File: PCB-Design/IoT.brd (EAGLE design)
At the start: 59.7 x 51.7 mm, 11 parts, among them M2 ARDUINO-NANO-3.0, M3 WIRELESS-NRF24L01

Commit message: PCB edit
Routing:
- net N$15: track 41.6 -> 39.6 mm
- net VCC: track 78.5 -> 76.5 mm
- net GND: track 105.4 -> 104.3 mm
- net N$9: track 50.2 -> 49.4 mm
- net N$13: track 17.7 -> 16.9 mm
- net N$12: track 17.7 -> 16.9 mm
- added copper zone on layer 1, net GND
- added copper zone on layer 16, net GND

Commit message: Redone PCB on bottom only
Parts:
- C1, C2: value (none) -> 10U/35V; device resistor:C025-040X050 -> capacitors-electrolytic:E2-5
- moved U$6 51.4 mm to (5.08, 78.7), turned to 0 degrees
- moved C1 14.0 mm to (24.1, 83.8), turned to 0 degrees
- moved HC-SR04-1 10.5 mm to (16.5, 55.9)
- moved M2 10.2 mm to (33.0, 69.8)
- moved HC-SR04-2 9.25 mm to (27.9, 55.9)
- moved HC-SR04-3 8.03 mm to (39.4, 55.9)
- moved C2 7.62 mm to (24.1, 94.0), turned to 0 degrees
- moved HC-SR04-4 6.84 mm to (50.8, 55.9)
- moved R1 3.81 mm to (19.1, 88.9)
- moved M3 2.84 mm to (43.2, 88.9)
- moved U$5 2.54 mm to (7.62, 92.7)
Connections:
- removed net N$4: C1.1, C2.1, M2.J2.14, M3.2
- new net N$2: C1.+, C2.+, M2.J2.14, M3.2
- net GND: now also C1.-, C2.-; no longer C1.2, C2.2
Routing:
- net GND: track 104.3 -> 0.00 mm, vias 1 -> 0
- net N$9: track 49.4 -> 147.9 mm
- net N$2: track 0.00 -> 47.6 mm
- net N$4: track 34.7 -> 0.00 mm
- net VCC: track 76.5 -> 104.5 mm
- net N$16: track 18.7 -> 30.2 mm
- net N$17: track 31.9 -> 43.2 mm
- net N$15: track 39.6 -> 46.7 mm
- net N$11: track 12.3 -> 7.40 mm
- net N$10: track 12.3 -> 7.40 mm
- net N$1: track 51.1 -> 46.2 mm
- net N$12: track 16.9 -> 12.3 mm
- net N$14: track 18.1 -> 22.5 mm
- net N$8: track 11.2 -> 7.93 mm
- net N$7: track 11.2 -> 7.93 mm
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- removed copper zone on layer 1, net GND
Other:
- board size 59.7 x 51.7 mm -> 60.9 x 49.2 mm

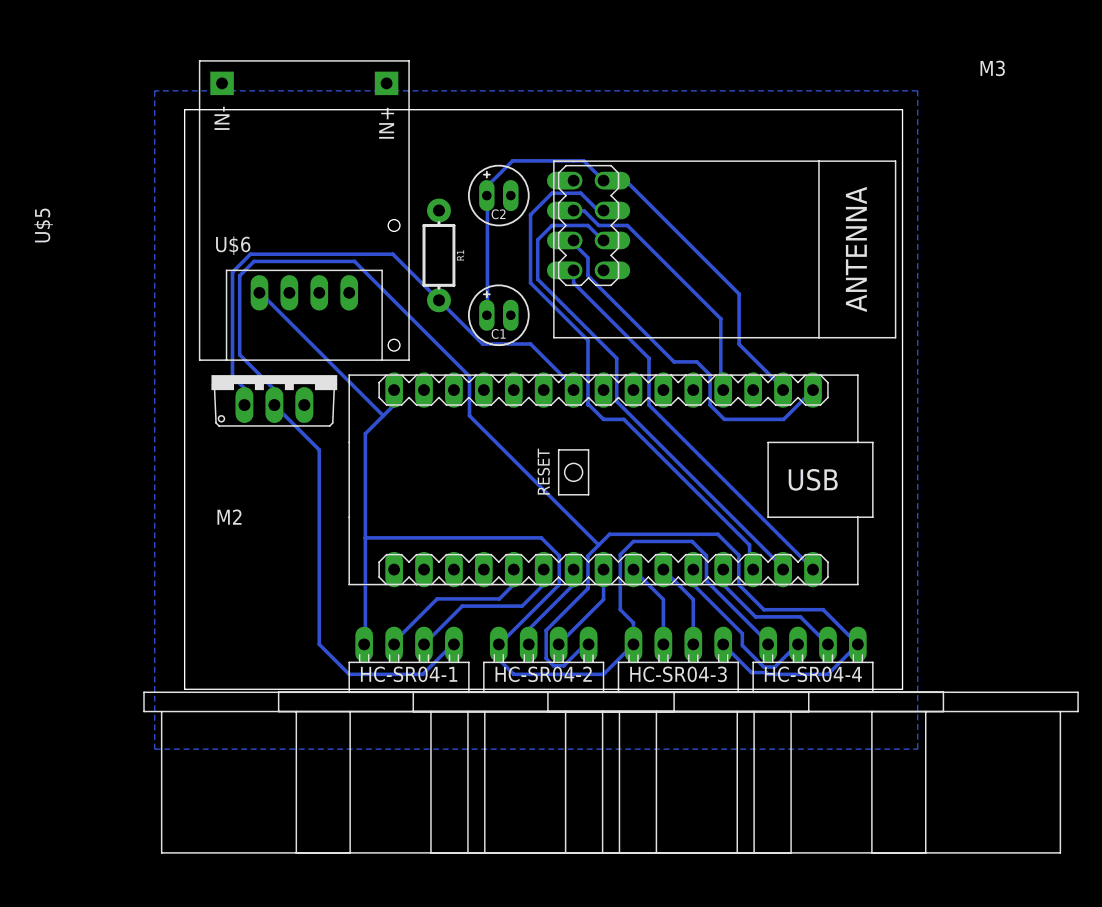
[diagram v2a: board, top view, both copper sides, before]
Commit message: New PCB no wires necessary
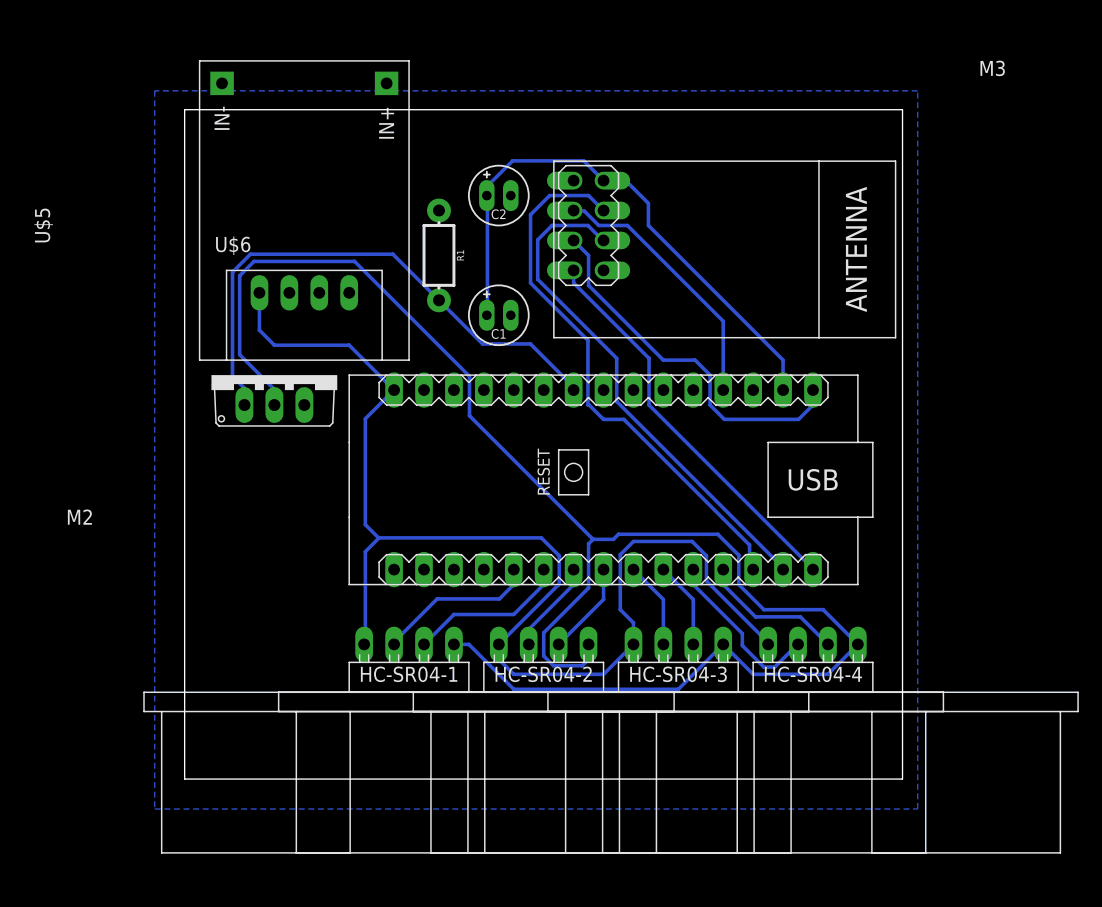
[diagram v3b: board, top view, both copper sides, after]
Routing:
- net N$9: track 147.9 -> 139.3 mm
- net VCC: track 104.5 -> 106.4 mm
- net N$16: track 30.2 -> 31.4 mm
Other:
- board size 60.9 x 49.2 mm -> 60.9 x 56.8 mm
- board text added: "Wits ParkSmart IoT"

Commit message: PCB edit
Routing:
- net N$9: track 139.3 -> 140.4 mm
- net VCC: track 106.4 -> 107.2 mm
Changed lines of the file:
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@@
 <layer number="19" name="Unrouted" color="6" fill="1" visible="yes" active="yes"/>
 <layer number="20" name="Dimension" color="24" fill="1" visible="yes" active="yes"/>
-<layer number="21" name="tPlace" color="7" fill="1" visible="yes" active="yes"/>
-<layer number="22" name="bPlace" color="7" fill="1" visible="yes" active="yes"/>
+<layer number="21" name="tPlace" color="7" fill="1" visible="no" active="yes"/>
+<layer number="22" name="bPlace" color="7" fill="1" visible="no" active="yes"/>
 <layer number="23" name="tOrigins" color="15" fill="1" visible="yes" active="yes"/>
 <layer number="24" name="bOrigins" color="15" fill="1" visible="yes" active="yes"/>
-<layer number="25" name="tNames" color="7" fill="1" visible="yes" active="yes"/>
+<layer number="25" name="tNames" color="7" fill="1" visible="no" active="yes"/>
 <layer number="26" name="bNames" color="7" fill="1" visible="yes" active="yes"/>
-<layer number="27" name="tValues" color="7" fill="1" visible="yes" active="yes"/>
-<layer number="28" name="bValues" color="7" fill="1" visible="yes" active="yes"/>
+<layer number="27" name="tValues" color="7" fill="1" visible="no" active="yes"/>
+<layer number="28" name="bValues" color="7" fill="1" visible="no" active="yes"/>
 <layer number="29" name="tStop" color="7" fill="3" visible="no" active="yes"/>
 <layer number="30" name="bStop" color="7" fill="6" visible="no" active="yes"/>
@@
 <contactref element="HC-SR04-1" pad="4"/>
 <contactref element="U$6" pad="2"/>
-<wire x1="46.6344" y1="58.8264" x2="44.5008" y2="60.96" width="0.3048" layer="16"/>
-<wire x1="54.5592" y1="55.7784" x2="54.61" y2="55.88" width="0.3048" layer="16"/>
-<wire x1="21.6408" y1="78.6384" x2="21.6408" y2="75.2856" width="0.3048" layer="16"/>
-<wire x1="11.8872" y1="88.392" x2="21.6408" y2="78.6384" width="0.3048" layer="16"/>
+<wire x1="21.6408" y1="78.6384" x2="11.8872" y2="88.392" width="0.3048" layer="16"/>
 <wire x1="3.3528" y1="88.392" x2="11.8872" y2="88.392" width="0.3048" layer="16"/>
 <wire x1="2.1336" y1="87.1728" x2="3.3528" y2="88.392" width="0.3048" layer="16"/>
@@
 <wire x1="2.1336" y1="80.4672" x2="5.08" y2="77.5208" width="0.3048" layer="16"/>
 <wire x1="5.08" y1="77.5208" x2="5.08" y2="76.2" width="0.3048" layer="16"/>
-<wire x1="44.5008" y1="63.4492" x2="44.5008" y2="60.96" width="0.3048" layer="16"/>
+<wire x1="44.5008" y1="60.96" x2="44.5008" y2="63.4492" width="0.3048" layer="16"/>
 <wire x1="42.7228" y1="65.2272" x2="44.5008" y2="63.4492" width="0.3048" layer="16"/>
-<wire x1="52.07" y1="53.34" x2="54.5084" y2="55.7784" width="0.3048" layer="16"/>
-<wire x1="54.5084" y1="55.7784" x2="54.5592" y2="55.7784" width="0.3048" layer="16"/>
-<wire x1="54.61" y1="55.88" x2="51.6636" y2="58.8264" width="0.3048" layer="16"/>
-<wire x1="51.6636" y1="58.8264" x2="46.6344" y2="58.8264" width="0.3048" layer="16"/>
 <wire x1="31.75" y1="55.88" x2="31.75" y2="54.61" width="0.3048" layer="16"/>
 <wire x1="28.771425" y1="54.0672" x2="27.94" y2="54.898625" width="0.3048" layer="16"/>
@@
 <wire x1="31.2072" y1="54.0672" x2="31.75" y2="54.61" width="0.3048" layer="16"/>
 <wire x1="43.18" y1="55.88" x2="45.72" y2="53.34" width="0.3048" layer="16"/>
-<wire x1="45.72" y1="53.34" x2="52.07" y2="53.34" width="0.3048" layer="16"/>
-<wire x1="39.37" y1="52.07" x2="43.18" y2="55.88" width="0.3048" layer="16"/>
-<wire x1="25.4" y1="52.07" x2="39.37" y2="52.07" width="0.3048" layer="16"/>
+<wire x1="43.18" y1="55.88" x2="40.005" y2="52.705" width="0.3048" layer="16"/>
 <wire x1="20.32" y1="55.88" x2="21.59" y2="55.88" width="0.3048" layer="16"/>
-<wire x1="21.59" y1="55.88" x2="25.4" y2="52.07" width="0.3048" layer="16"/>
-<wire x1="21.6408" y1="75.2856" x2="32.131" y2="64.7954" width="0.3048" layer="16"/>
+<wire x1="24.765" y1="52.705" x2="21.59" y2="55.88" width="0.3048" layer="16"/>
 <wire x1="34.29" y1="65.2272" x2="42.7228" y2="65.2272" width="0.3048" layer="16"/>
-<wire x1="31.75" y1="64.4144" x2="32.131" y2="64.7954" width="0.3048" layer="16"/>
 <wire x1="27.94" y1="56.861375" x2="31.75" y2="60.671375" width="0.3048" layer="16"/>
-<wire x1="31.75" y1="60.671375" x2="31.75" y2="64.4144" width="0.3048" layer="16"/>
-<wire x1="33.8582" y1="64.7954" x2="34.29" y2="65.2272" width="0.3048" layer="16"/>
-<wire x1="32.131" y1="64.7954" x2="33.8582" y2="64.7954" width="0.3048" layer="16"/>
+<wire x1="31.75" y1="60.671375" x2="31.75" y2="63.5" width="0.3048" layer="16"/>
+<wire x1="31.75" y1="63.5" x2="32.385" y2="64.135" width="0.3048" layer="16"/>
+<wire x1="32.385" y1="64.135" x2="33.02" y2="64.77" width="0.3048" layer="16"/>
+<wire x1="33.02" y1="64.77" x2="33.4772" y2="65.2272" width="0.3048" layer="16"/>
+<wire x1="33.4772" y1="65.2272" x2="34.29" y2="65.2272" width="0.3048" layer="16"/>
+<wire x1="32.385" y1="64.135" x2="21.6408" y2="74.8792" width="0.3048" layer="16"/>
+<wire x1="21.6408" y1="74.8792" x2="21.6408" y2="78.6384" width="0.3048" layer="16"/>
+<wire x1="40.005" y1="52.705" x2="24.765" y2="52.705" width="0.3048" layer="16"/>
+<wire x1="53.34" y1="53.34" x2="54.61" y2="54.61" width="0.3048" layer="16"/>
+<wire x1="54.61" y1="54.61" x2="54.61" y2="55.88" width="0.3048" layer="16"/>
+<wire x1="45.72" y1="53.34" x2="53.34" y2="53.34" width="0.3048" layer="16"/>
+<wire x1="54.61" y1="55.88" x2="54.61" y2="57.15" width="0.3048" layer="16"/>
+<wire x1="52.07" y1="59.69" x2="45.7708" y2="59.69" width="0.3048" layer="16"/>
+<wire x1="54.61" y1="57.15" x2="52.07" y2="59.69" width="0.3048" layer="16"/>
+<wire x1="45.7708" y1="59.69" x2="44.5008" y2="60.96" width="0.3048" layer="16"/>
 </signal>
 <signal name="N$14">
@@
 <contactref element="HC-SR04-2" pad="3"/>
 <contactref element="M2" pad="J1.8"/>
-<wire x1="29.21" y1="55.88" x2="33.02" y2="59.69" width="0.3048" layer="16"/>
-<wire x1="33.02" y1="59.69" x2="33.02" y2="62.23" width="0.3048" layer="16"/>
+<wire x1="33.02" y1="60.96" x2="33.02" y2="62.23" width="0.3048" layer="16"/>
+<wire x1="29.21" y1="55.88" x2="29.21" y2="57.15" width="0.3048" layer="16"/>
+<wire x1="29.21" y1="57.15" x2="33.02" y2="60.96" width="0.3048" layer="16"/>
 </signal>
 <signal name="N$8">
@@
 <contactref element="M2" pad="J1.11"/>
 <wire x1="47.5488" y1="53.9496" x2="49.3776" y2="55.7784" width="0.3048" layer="16"/>
-<wire x1="46.6344" y1="53.9496" x2="47.5488" y2="53.9496" width="0.3048" layer="16"/>
-<wire x1="44.8056" y1="55.7784" x2="46.6344" y2="53.9496" width="0.3048" layer="16"/>
 <wire x1="49.3776" y1="55.7784" x2="49.53" y2="55.88" width="0.3048" layer="16"/>
 <wire x1="40.64" y1="62.23" x2="40.64" y2="60.96" width="0.3048" layer="16"/>
-<wire x1="40.64" y1="60.96" x2="44.8056" y2="56.7944" width="0.3048" layer="16"/>
-<wire x1="44.8056" y1="56.7944" x2="44.8056" y2="55.7784" width="0.3048" layer="16"/>
+<wire x1="40.64" y1="60.96" x2="44.45" y2="57.15" width="0.3048" layer="16"/>
+<wire x1="44.45" y1="57.15" x2="44.45" y2="55.88" width="0.3048" layer="16"/>
+<wire x1="44.45" y1="55.88" x2="46.3804" y2="53.9496" width="0.3048" layer="16"/>
+<wire x1="46.3804" y1="53.9496" x2="47.5488" y2="53.9496" width="0.3048" layer="16"/>
 </signal>
 <signal name="GND">
@@
 <contactref element="HC-SR04-3" pad="1"/>
 <contactref element="HC-SR04-4" pad="1"/>
-<wire x1="41.7576" y1="61.2648" x2="46.9392" y2="56.0832" width="0.3048" layer="16"/>
-<wire x1="41.7576" y1="63.3984" x2="41.7576" y2="61.2648" width="0.3048" layer="16"/>
-<wire x1="40.5384" y1="64.6176" x2="41.7576" y2="63.3984" width="0.3048" layer="16"/>
+<wire x1="41.7576" y1="63.3984" x2="40.5384" y2="64.6176" width="0.3048" layer="16"/>
 <wire x1="35.56" y1="64.6176" x2="40.5384" y2="64.6176" width="0.3048" layer="16"/>
 <wire x1="34.4424" y1="58.8264" x2="34.4424" y2="63.5" width="0.3048" layer="16"/>
-<wire x1="46.9392" y1="56.0832" x2="46.99" y2="55.88" width="0.3048" layer="16"/>
 <wire x1="12.8016" y1="63.754" x2="12.8016" y2="56.0832" width="0.3048" layer="16"/>
 <wire x1="12.8016" y1="56.0832" x2="12.7" y2="55.88" width="0.3048" layer="16"/>
@@
 <wire x1="35.56" y1="57.7088" x2="34.4424" y2="58.8264" width="0.3048" layer="16"/>
 <wire x1="35.56" y1="55.88" x2="35.56" y2="57.7088" width="0.3048" layer="16"/>
-<wire x1="33.02" y1="53.34" x2="35.56" y2="55.88" width="0.3048" layer="16"/>
 <wire x1="24.13" y1="55.88" x2="29.21" y2="60.96" width="0.3048" layer="16"/>
 <wire x1="29.21" y1="60.96" x2="29.2608" y2="60.96" width="0.3048" layer="16"/>
 <wire x1="24.13" y1="55.88" x2="24.13" y2="54.61" width="0.3048" layer="16"/>
 <wire x1="24.13" y1="54.61" x2="25.4" y2="53.34" width="0.3048" layer="16"/>
-<wire x1="25.4" y1="53.34" x2="33.02" y2="53.34" width="0.3048" layer="16"/>
 <wire x1="12.8016" y1="63.754" x2="13.97" y2="64.9224" width="0.3048" layer="16"/>
 <wire x1="13.97" y1="64.9224" x2="13.9192" y2="64.9224" width="0.3048" layer="16"/>
@@
 <wire x1="15.24" y1="77.47" x2="12.8016" y2="75.0316" width="0.3048" layer="16"/>
 <wire x1="12.8016" y1="75.0316" x2="12.8016" y2="66.04" width="0.3048" layer="16"/>
+<wire x1="46.99" y1="55.88" x2="41.7576" y2="61.1124" width="0.3048" layer="16"/>
+<wire x1="41.7576" y1="61.1124" x2="41.7576" y2="63.3984" width="0.3048" layer="16"/>
+<wire x1="34.29" y1="53.34" x2="35.56" y2="54.61" width="0.3048" layer="16"/>
+<wire x1="35.56" y1="54.61" x2="35.56" y2="55.88" width="0.3048" layer="16"/>
+<wire x1="25.4" y1="53.34" x2="34.29" y2="53.34" width="0.3048" layer="16"/>
 </signal>
 <signal name="N$2">
